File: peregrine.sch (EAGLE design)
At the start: 75 parts, among them Q1 BSS123, Q10 BSS123, Q11 BSS123, Q2 BSS123, U1 ITG-3200, U2 ADXL345, U5 ATMEGA32U4-XUAU, X2 USB-MICROB, Y1 16MHz KX-7

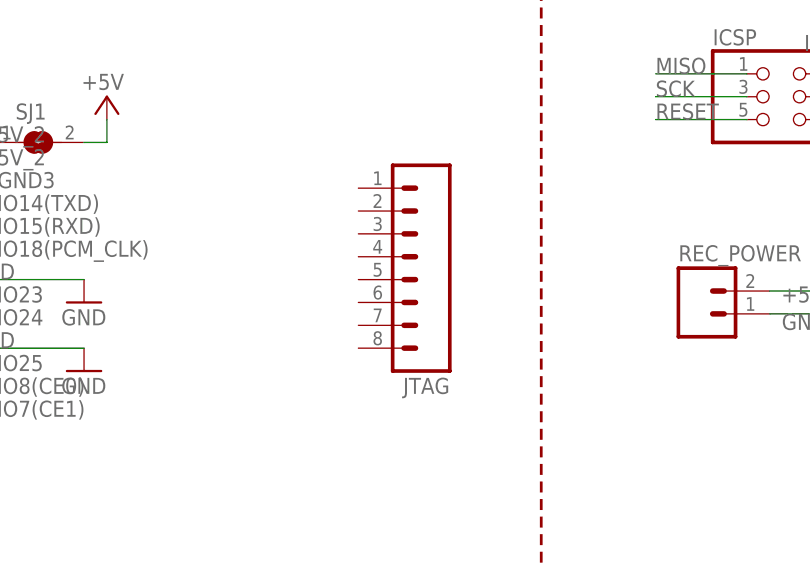
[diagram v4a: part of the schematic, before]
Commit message: Added notch for RCA connector
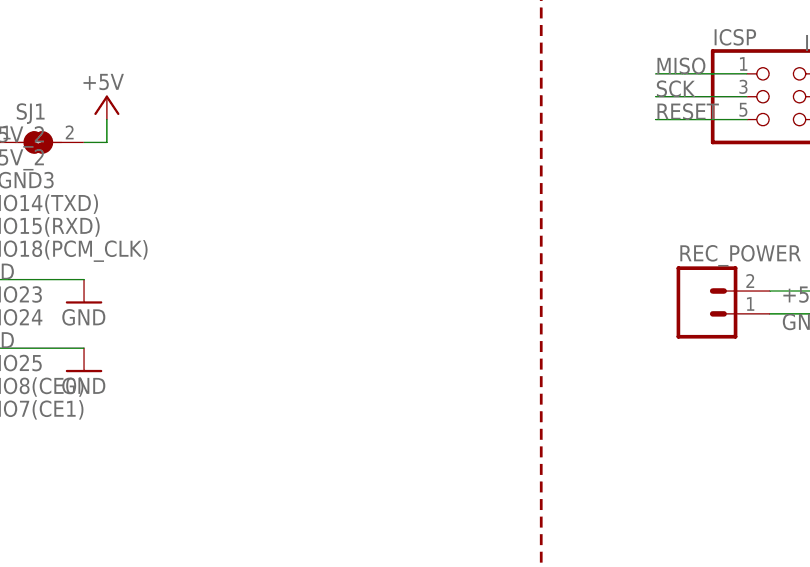
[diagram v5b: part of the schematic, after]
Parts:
- removed JTAG: (no value), SparkFun:M08LOCK
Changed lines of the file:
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@@
 <part name="C14" library="SparkFun" deviceset="CAP" device="0402-CAP" value="0.1uF"/>
 <part name="GND16" library="SparkFun" deviceset="GND" device=""/>
-<part name="JTAG" library="SparkFun" deviceset="M08" device="LOCK"/>
 <part name="SJ5" library="jumper" deviceset="SJ" device=""/>
 <part name="SJ6" library="jumper" deviceset="SJ" device=""/>
@@
 </instance>
 <instance part="GND16" gate="1" x="-15.24" y="-43.18"/>
-<instance part="JTAG" gate="G$1" x="124.46" y="83.82" rot="R180"/>
 <instance part="SJ5" gate="1" x="231.14" y="48.26"/>
 <instance part="SJ6" gate="1" x="231.14" y="43.18"/>

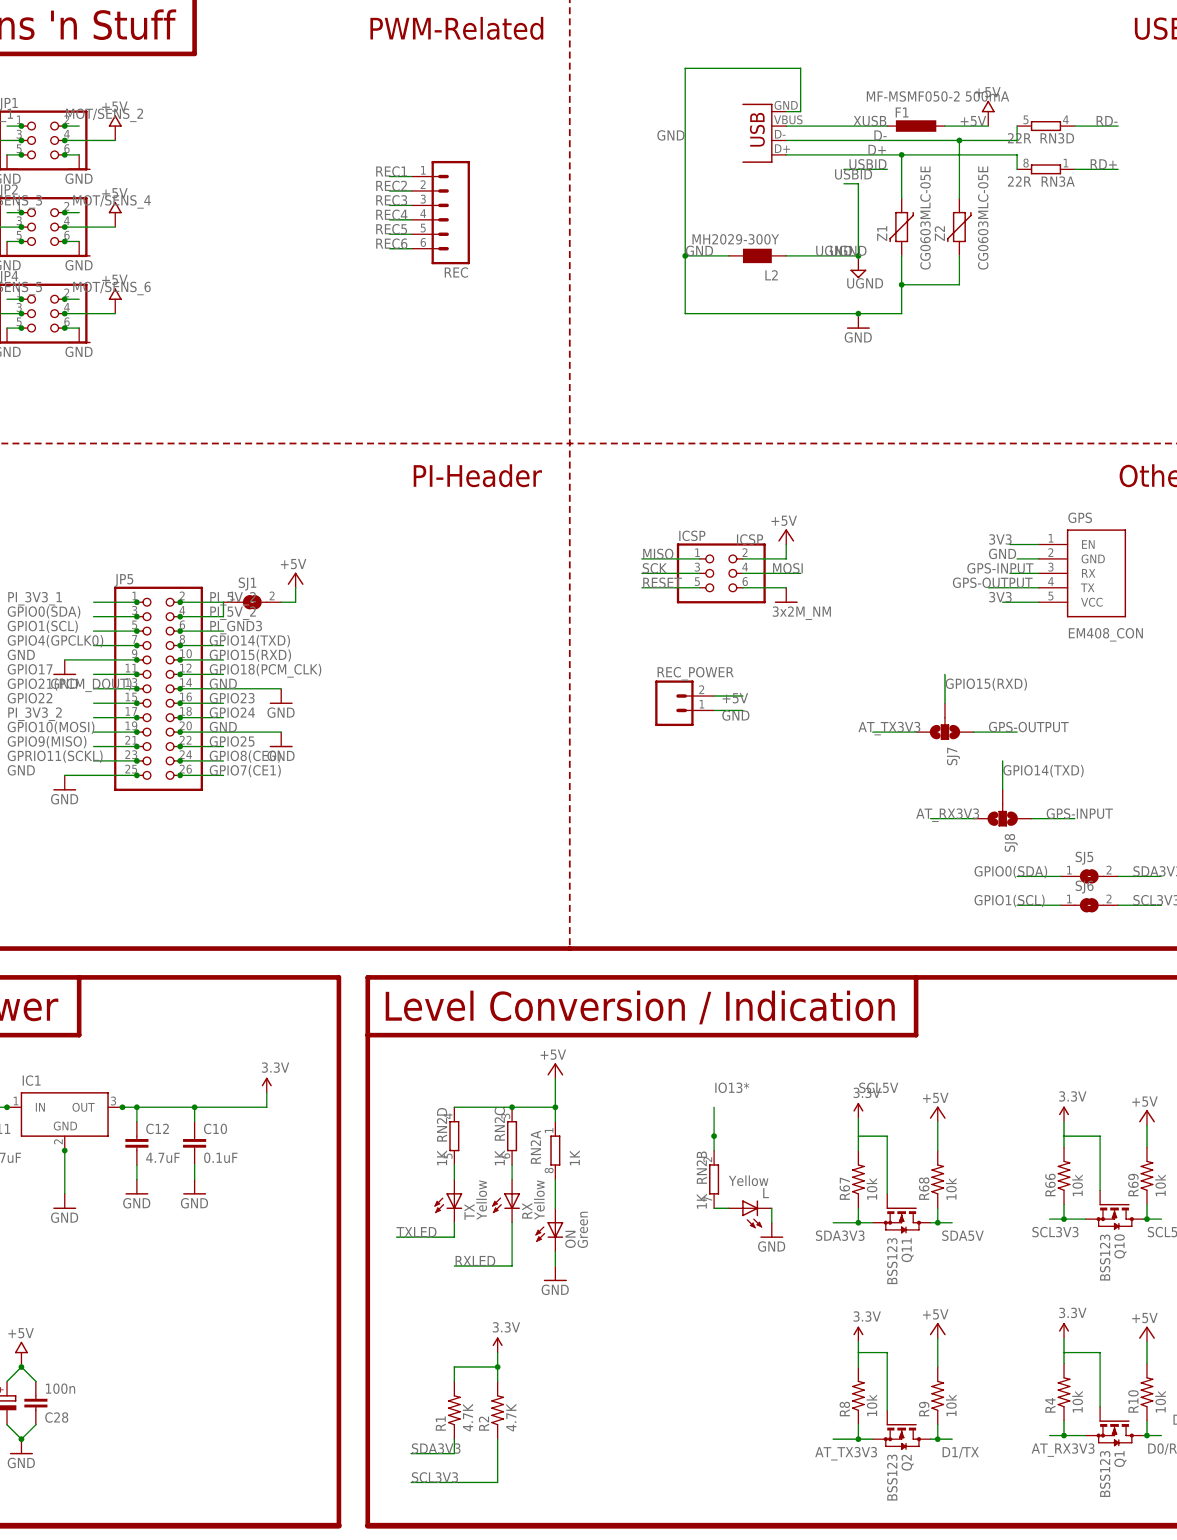
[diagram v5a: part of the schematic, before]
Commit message: Changed outline, removed unused parts, via stops
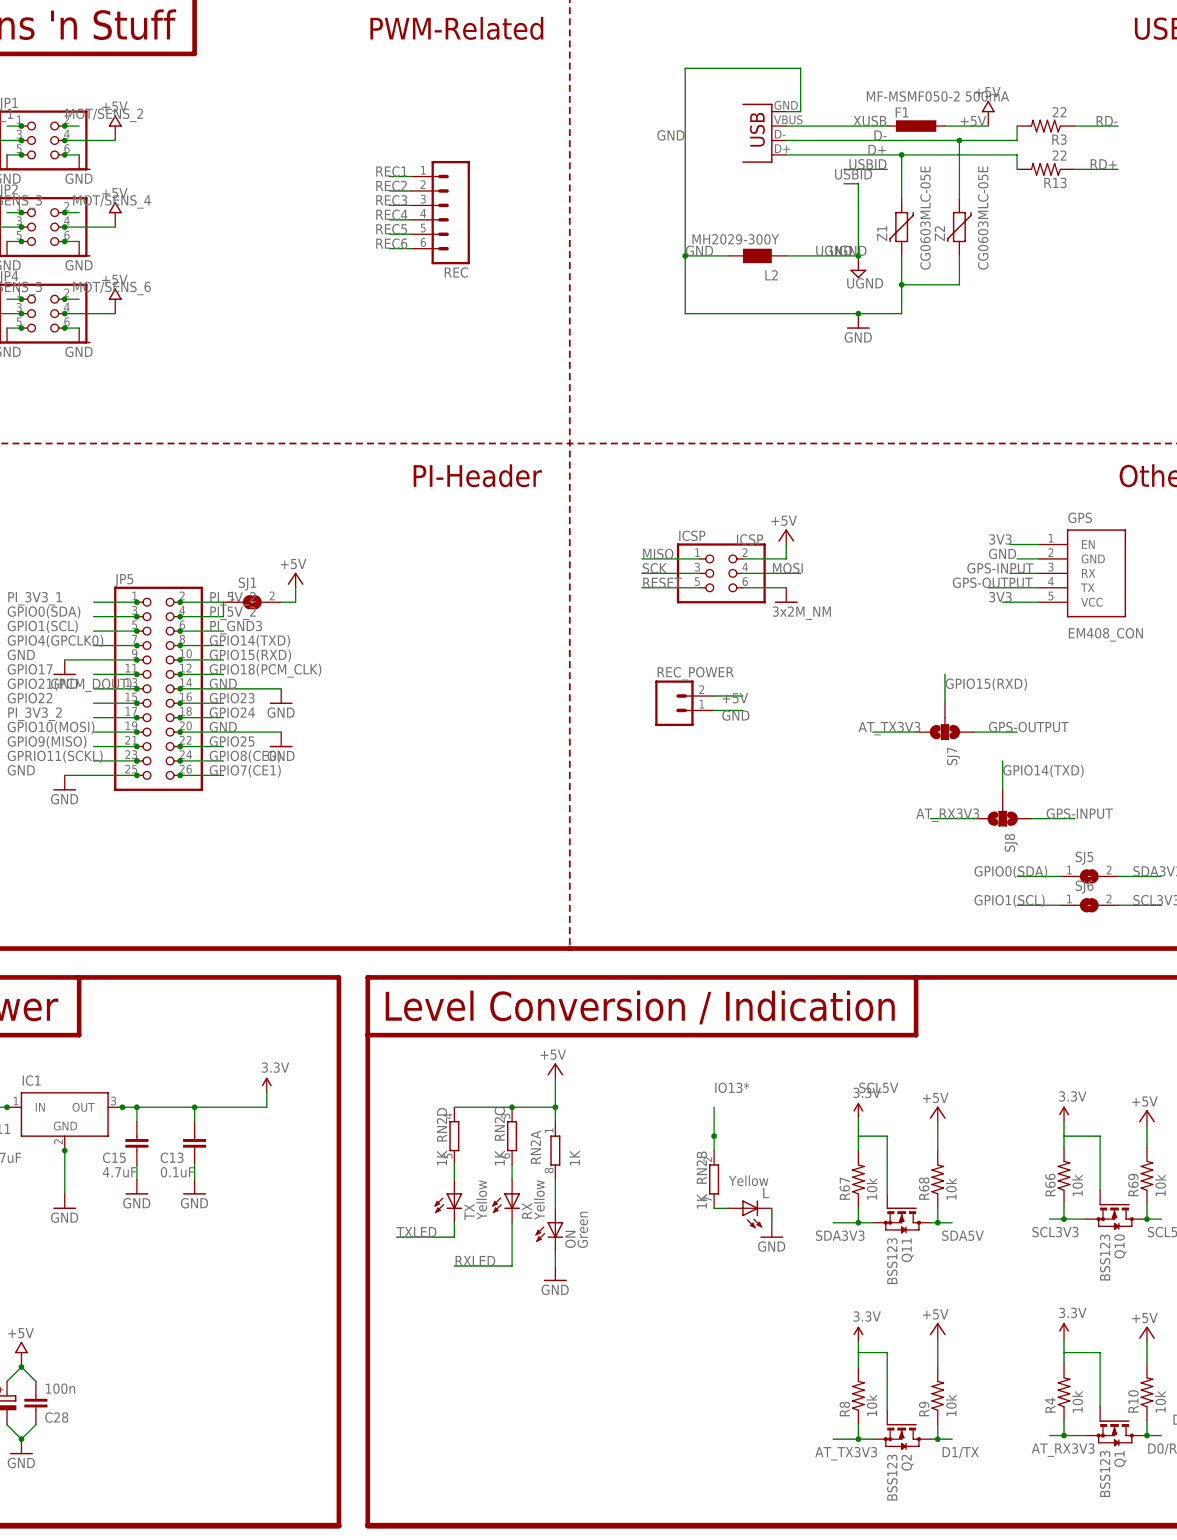
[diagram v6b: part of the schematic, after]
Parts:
- removed R1, R2: 4.7K, SparkFun:RESISTOR0402-RES
- removed RN3: 22R, resistor-dil:4R-NCAY16
- added R13, R3: 22, SparkFun:RESISTOR0603-RES
- renumbered C10 to C13, C12 to C15
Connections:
- net 3V3: no longer R1.2, R2.2
- net D+: now also R13.2; no longer RN3A.2
- net D-: now also R3.2; no longer RN3D.2
- net RD+: now also R13.1; no longer RN3A.1
- net RD-: now also R3.1; no longer RN3D.1
- net SCL3V3: no longer R2.1
- net SDA3V3: no longer R1.1
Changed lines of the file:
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@@
 <part name="GND10" library="SparkFun" deviceset="GND" device=""/>
 <part name="GND11" library="SparkFun" deviceset="GND" device=""/>
-<part name="C10" library="SparkFun" deviceset="CAP" device="0402-CAP" value="0.1uF"/>
 <part name="GND12" library="SparkFun" deviceset="GND" device=""/>
-<part name="R1" library="SparkFun" deviceset="RESISTOR" device="0402-RES" value="4.7K"/>
-<part name="R2" library="SparkFun" deviceset="RESISTOR" device="0402-RES" value="4.7K"/>
-<part name="P+9" library="SparkFun" deviceset="3.3V" device=""/>
-<part name="C12" library="SparkFun" deviceset="CAP" device="0402-CAP" value="4.7uF"/>
 <part name="GND9" library="SparkFun" deviceset="GND" device=""/>
 <part name="C11" library="SparkFun" deviceset="CAP" device="0402-CAP" value="4.7uF"/>
@@
 <part name="SUPPLY2" library="supply2" deviceset="GND1" device="" value="UGND"/>
 <part name="U$30" library="MyPOW" deviceset="COM" device=""/>
-<part name="RN3" library="resistor-dil" deviceset="4R-N" device="CAY16" value="22R"/>
 <part name="C23" library="SmartPrj" deviceset="C-EU" device="C0603" value="1uF"/>
 <part name="U$36" library="MyPOW" deviceset="+5V" device=""/>
@@
 <part name="GND19" library="SparkFun" deviceset="GND" device=""/>
 <part name="X2" library="SparkFun" deviceset="USB" device="-MICROB"/>
+<part name="R3" library="SparkFun" deviceset="RESISTOR" device="0603-RES" value="22"/>
+<part name="R13" library="SparkFun" deviceset="RESISTOR" device="0603-RES" value="22"/>
+<part name="C13" library="SparkFun" deviceset="CAP" device="0402-CAP" value="0.1uF"/>
+<part name="C15" library="SparkFun" deviceset="CAP" device="0402-CAP" value="4.7uF"/>
 </parts>
 <sheets>
@@
 <instance part="GND10" gate="1" x="-88.9" y="-43.18"/>
 <instance part="GND11" gate="1" x="50.8" y="-10.16"/>
-<instance part="C10" gate="G$1" x="73.66" y="0"/>
 <instance part="GND12" gate="1" x="73.66" y="-7.62"/>
-<instance part="R1" gate="G$1" x="119.38" y="-45.72" rot="R90"/>
-<instance part="R2" gate="G$1" x="127" y="-45.72" rot="R90"/>
-<instance part="P+9" gate="G$1" x="127" y="-35.56"/>
-<instance part="C12" gate="G$1" x="63.5" y="0"/>
 <instance part="GND9" gate="1" x="63.5" y="-7.62"/>
 <instance part="C11" gate="G$1" x="35.56" y="0"/>
@@
 <instance part="SUPPLY2" gate="G$1" x="-86.36" y="88.9"/>
 <instance part="U$30" gate="G$1" x="-81.28" y="99.06"/>
-<instance part="RN3" gate="A" x="223.52" y="172.72" rot="MR0"/>
-<instance part="RN3" gate="D" x="223.52" y="180.34" rot="MR0"/>
 <instance part="C23" gate="G$1" x="-86.36" y="116.84"/>
 <instance part="U$36" gate="G$1" x="-81.28" y="167.64"/>
@@
 <instance part="GND19" gate="1" x="88.9" y="78.74"/>
 <instance part="X2" gate="G$1" x="175.26" y="182.88" rot="R180"/>
+<instance part="R3" gate="G$1" x="223.52" y="180.34" rot="R180"/>
+<instance part="R13" gate="G$1" x="223.52" y="172.72" rot="R180"/>
+<instance part="C13" gate="G$1" x="73.66" y="0" smashed="yes">
+<attribute name="NAME" x="67.564" y="-2.159" size="1.778" layer="95"/>
+<attribute name="VALUE" x="67.564" y="-4.699" size="1.778" layer="96"/>
+</instance>
+<instance part="C15" gate="G$1" x="63.5" y="0" smashed="yes">
+<attribute name="NAME" x="57.404" y="-2.159" size="1.778" layer="95"/>
+<attribute name="VALUE" x="57.404" y="-4.699" size="1.778" layer="96"/>
+</instance>
 </instances>
 <busses>
@@
 <wire x1="73.66" y1="-5.08" x2="73.66" y2="-2.54" width="0.1524" layer="91"/>
 <pinref part="GND12" gate="1" pin="GND"/>
-<pinref part="C10" gate="G$1" pin="2"/>
+<pinref part="C13" gate="G$1" pin="2"/>
 </segment>
 <segment>
 <wire x1="63.5" y1="-5.08" x2="63.5" y2="-2.54" width="0.1524" layer="91"/>
-<pinref part="C12" gate="G$1" pin="2"/>
 <pinref part="GND9" gate="1" pin="GND"/>
+<pinref part="C15" gate="G$1" pin="2"/>
 </segment>
 <segment>
@@
 <junction x="63.5" y="7.62"/>
 <junction x="73.66" y="7.62"/>
-<pinref part="C10" gate="G$1" pin="1"/>
-<pinref part="C12" gate="G$1" pin="1"/>
 <pinref part="P+11" gate="G$1" pin="3.3V"/>
 <pinref part="IC1" gate="G$1" pin="OUT"/>
 <junction x="60.96" y="7.62"/>
-</segment>
-<segment>
-<wire x1="119.38" y1="-40.64" x2="119.38" y2="-38.1" width="0.1524" layer="91"/>
-<wire x1="119.38" y1="-38.1" x2="127" y2="-38.1" width="0.1524" layer="91"/>
-<wire x1="127" y1="-38.1" x2="127" y2="-35.56" width="0.1524" layer="91"/>
-<wire x1="127" y1="-40.64" x2="127" y2="-38.1" width="0.1524" layer="91"/>
-<junction x="127" y="-38.1"/>
-<pinref part="R1" gate="G$1" pin="2"/>
-<pinref part="P+9" gate="G$1" pin="3.3V"/>
-<pinref part="R2" gate="G$1" pin="2"/>
+<pinref part="C15" gate="G$1" pin="1"/>
+<pinref part="C13" gate="G$1" pin="1"/>
 </segment>
 <segment>
@@
 <label x="195.58" y="177.8" size="1.778" layer="95" rot="MR0"/>
 <pinref part="Z2" gate="G$1" pin="1"/>
-<pinref part="RN3" gate="D" pin="2"/>
 <pinref part="X2" gate="G$1" pin="D-"/>
+<pinref part="R3" gate="G$1" pin="2"/>
 </segment>
 </net>
@@
 <label x="195.58" y="175.26" size="1.778" layer="95" rot="MR0"/>
 <pinref part="Z1" gate="G$1" pin="1"/>
-<pinref part="RN3" gate="A" pin="2"/>
 <pinref part="X2" gate="G$1" pin="D+"/>
 <wire x1="198.12" y1="175.26" x2="177.8" y2="175.26" width="0.1524" layer="91"/>
+<pinref part="R13" gate="G$1" pin="2"/>
 </segment>
 </net>
@@
 <wire x1="228.6" y1="180.34" x2="236.22" y2="180.34" width="0.1524" layer="91"/>
 <label x="236.22" y="180.34" size="1.778" layer="95" rot="MR0"/>
-<pinref part="RN3" gate="D" pin="1"/>
+<pinref part="R3" gate="G$1" pin="1"/>
 </segment>
 <segment>
@@
 <wire x1="228.6" y1="172.72" x2="236.22" y2="172.72" width="0.1524" layer="91"/>
 <label x="236.22" y="172.72" size="1.778" layer="95" rot="MR0"/>
-<pinref part="RN3" gate="A" pin="1"/>
+<pinref part="R13" gate="G$1" pin="1"/>
 </segment>
 <segment>
@@
 </segment>
 <segment>
-<wire x1="127" y1="-50.8" x2="127" y2="-58.42" width="0.1524" layer="91"/>
-<wire x1="127" y1="-58.42" x2="111.76" y2="-58.42" width="0.1524" layer="91"/>
-<label x="111.76" y="-58.42" size="1.778" layer="95"/>
-<pinref part="R2" gate="G$1" pin="1"/>
-</segment>
-<segment>
 <pinref part="SJ6" gate="1" pin="2"/>
 <wire x1="236.22" y1="43.18" x2="243.84" y2="43.18" width="0.1524" layer="91"/>
@@
 </segment>
 <segment>
-<wire x1="119.38" y1="-50.8" x2="119.38" y2="-53.34" width="0.1524" layer="91"/>
-<wire x1="119.38" y1="-53.34" x2="111.76" y2="-53.34" width="0.1524" layer="91"/>
-<label x="111.76" y="-53.34" size="1.778" layer="95"/>
-<pinref part="R1" gate="G$1" pin="1"/>
-</segment>
-<segment>
